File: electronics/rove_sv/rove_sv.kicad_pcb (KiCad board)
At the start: 2 copper layers, 60 x 50 mm, 27 parts, among them J1 USB-C, J2 Battery, J3 LeftMotor, J4 RightMotor, J5 Servo1, J6 Servo2, Q1 FS8205A, SW1 BOOT, U1 ESP32-S3-WROOM-1, U2 DRV8833PW, U3 XC6220B331MR, U5 DW01A

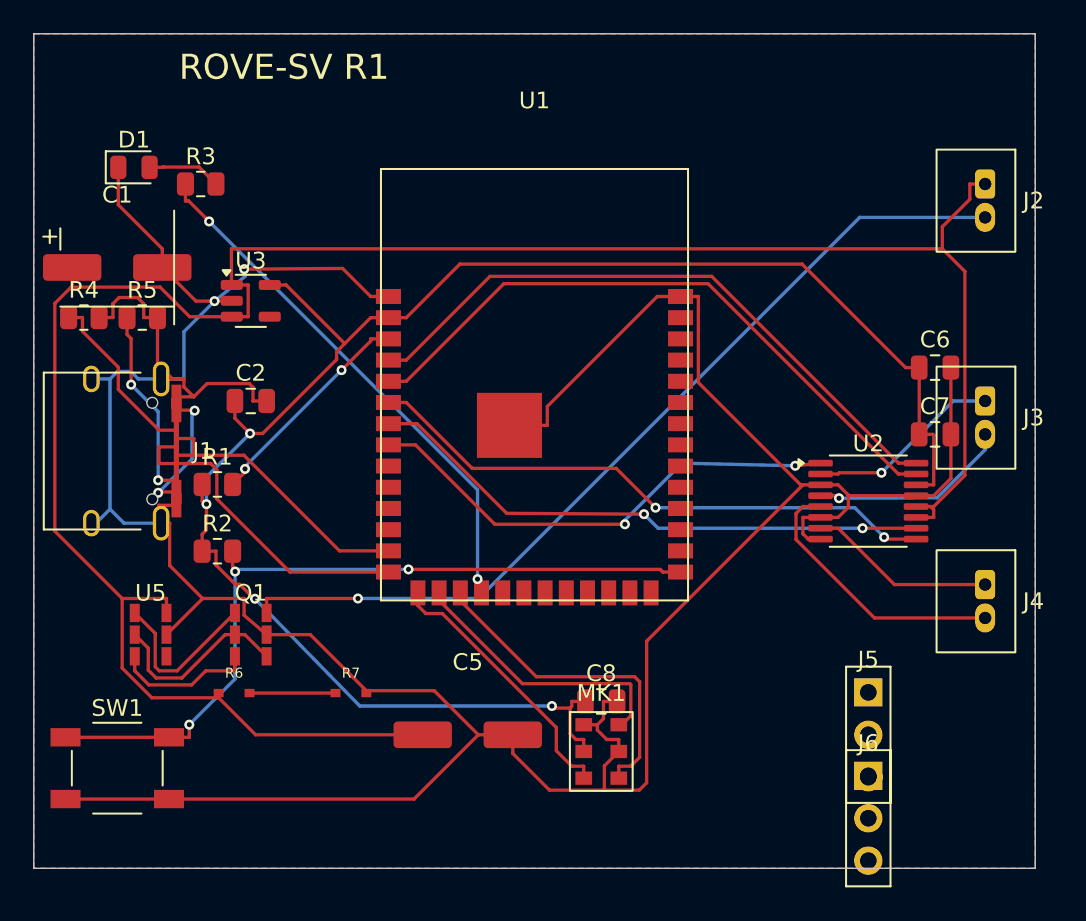
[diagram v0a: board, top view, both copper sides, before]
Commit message: ROVE-SV R1: PCB routed with servo connectors J5/J6
- Added J5 (SERVO1) at (50, 35mm) and J6 (SERVO2) at (50, 43mm)
- SERVO1 on GPIO12 (ESP32 pad 12), SERVO2 on GPIO11 (ESP32 pad 11)
- I2S microphone connections preserved on GPIO15/16/17
- 0 unconnected items after freerouting
- DRC: 189 violations (all J1 USB-C geometry or minor autorouter
  clearance issues — same class as ROVE-V pre-DRC-fix state)
- Gerbers: rove_sv_gerbers_r1_routed.zip

Co-Authored-By: Claude Sonnet 4.6 <noreply@anthropic.com>
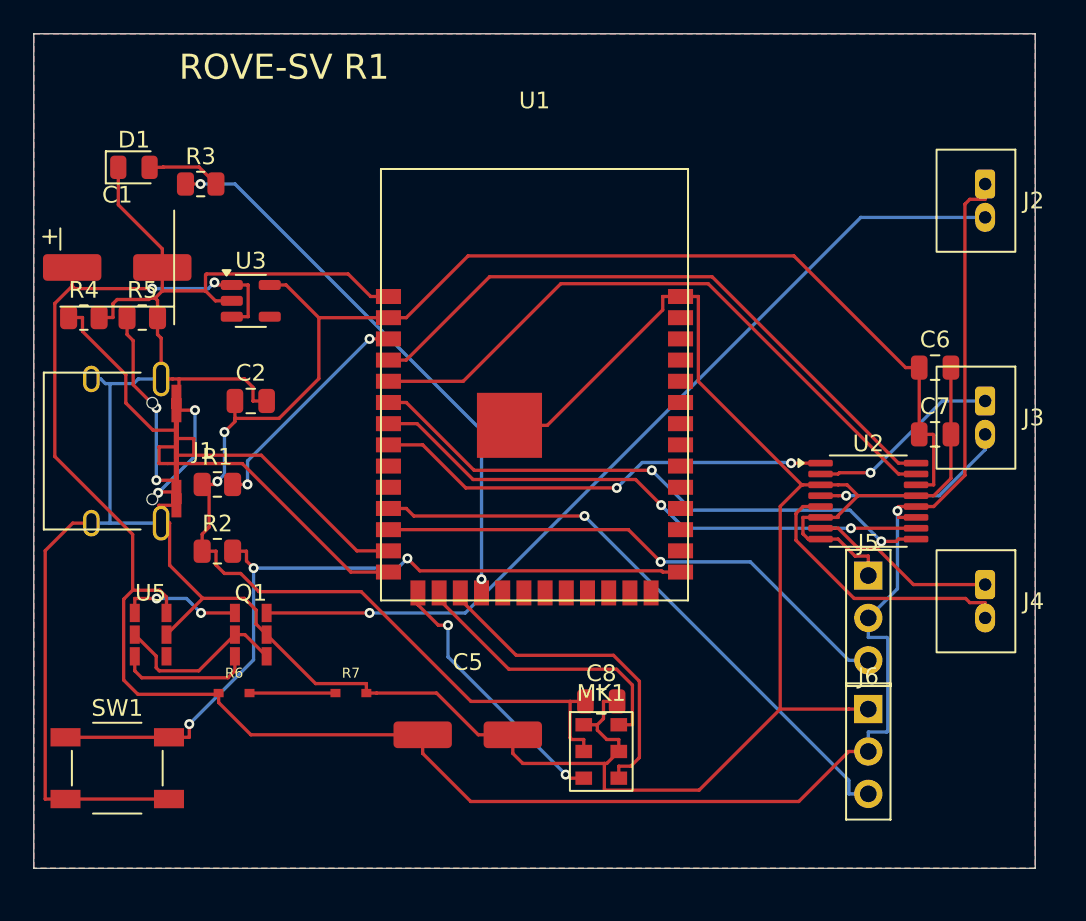
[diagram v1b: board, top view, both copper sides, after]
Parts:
- moved J5 7.00 mm to (50.0, 35.0)
- moved J6 4.00 mm to (50.0, 43.0)
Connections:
- J5 pad 2: VBAT -> /VBAT
- J5 pad 3: SERVO1 -> /SERVO1
- J6 pad 2: VBAT -> /VBAT
- J6 pad 3: SERVO2 -> /SERVO2
- U1 pad 11: (no net) -> /SERVO2
- U1 pad 12: (no net) -> /SERVO1
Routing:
- net /SERVO2: track 0.00 -> 36.3 mm, vias 0 -> 1
- net /SERVO1: track 0.00 -> 32.0 mm, vias 0 -> 1
- net GND: track 219.0 -> 223.4 mm, vias 2 -> 0
- net /VBAT: track 133.6 -> 136.5 mm, vias 0 -> 3
- net /DW01_OC: track 10.0 -> 7.23 mm, vias 0 -> 2
- net /DRV_SLEEP: track 29.5 -> 27.6 mm
- net /STATUS_LED: track 32.0 -> 33.6 mm
- net /USB_D+: track 19.5 -> 18.5 mm
- net /3V3: track 104.9 -> 104.0 mm, vias 4 -> 2
- net /IO0: track 46.6 -> 47.3 mm
- net /PROT_CS: track 11.4 -> 10.6 mm
- net /BOUT2: track 16.5 -> 17.0 mm
- net /EN: track 13.2 -> 13.8 mm
- net /BATT_NEG: track 53.4 -> 52.9 mm
- net /I2S_WS: track 16.2 -> 16.1 mm, vias 0 -> 2
